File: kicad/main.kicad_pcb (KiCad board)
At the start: 2 copper layers, 119.4 x 99.1 mm, 41 parts, among them J1 Barrel_Jack, SW1 Reset, SW6 SW_DIP_x08, U1 KM1810VM88, U10 L7805, U11 15 MHz, U12 8255, U13 74HC273, U14 74HC244, U2 W27C512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

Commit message: Mark as v02
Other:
- board text added: "Андрій Дунай v0.2, Вересень 2023 <a@dun.ai>"
- board text removed: "Андрій Дунай v0.1, Вересень 2023 <a@dun.ai>"
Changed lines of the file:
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@@
   (gr_rect (start 15.24 -109.22) (end 134.62 -10.16)
     (stroke (width 0.2) (type default)) (fill none) (layer "Edge.Cuts"))
-  (gr_text "Андрій Дунай\nv0.1, Вересень 2023\n<a@dun.ai>" (at 113.3475 -41.275) (layer "F.SilkS")
+  (gr_text "Андрій Дунай\nv0.2, Вересень 2023\n<a@dun.ai>" (at 113.3475 -41.275) (layer "F.SilkS")
     (effects (font (size 1 1) (thickness 0.15)) (justify left bottom))
   )

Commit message: Update PCB image
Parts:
- moved C10 128.3 mm to (114.3, 94.0)
- moved C2 128.3 mm to (43.2, 39.4)
- moved C3 128.3 mm to (27.9, 62.2)
- moved C4 128.3 mm to (90.2, 29.2)
- moved C5 128.3 mm to (90.2, 61.0)
- moved C6 128.3 mm to (110.5, 38.1)
- moved C8 128.3 mm to (116.8, 76.1)
- moved C9 128.3 mm to (85.1, 94.0)
- moved H1 128.3 mm to (21.6, 114.3)
- moved H2 128.3 mm to (133.3, 114.3)
- moved J1 128.3 mm to (128.9, 33.0)
- moved J2 128.3 mm to (20.3, 43.2)
- moved LCD1 128.3 mm to (20.3, 20.3)
- moved RN3 128.3 mm to (80.0, 102.9)
- moved RN4 128.3 mm to (109.2, 102.9)
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
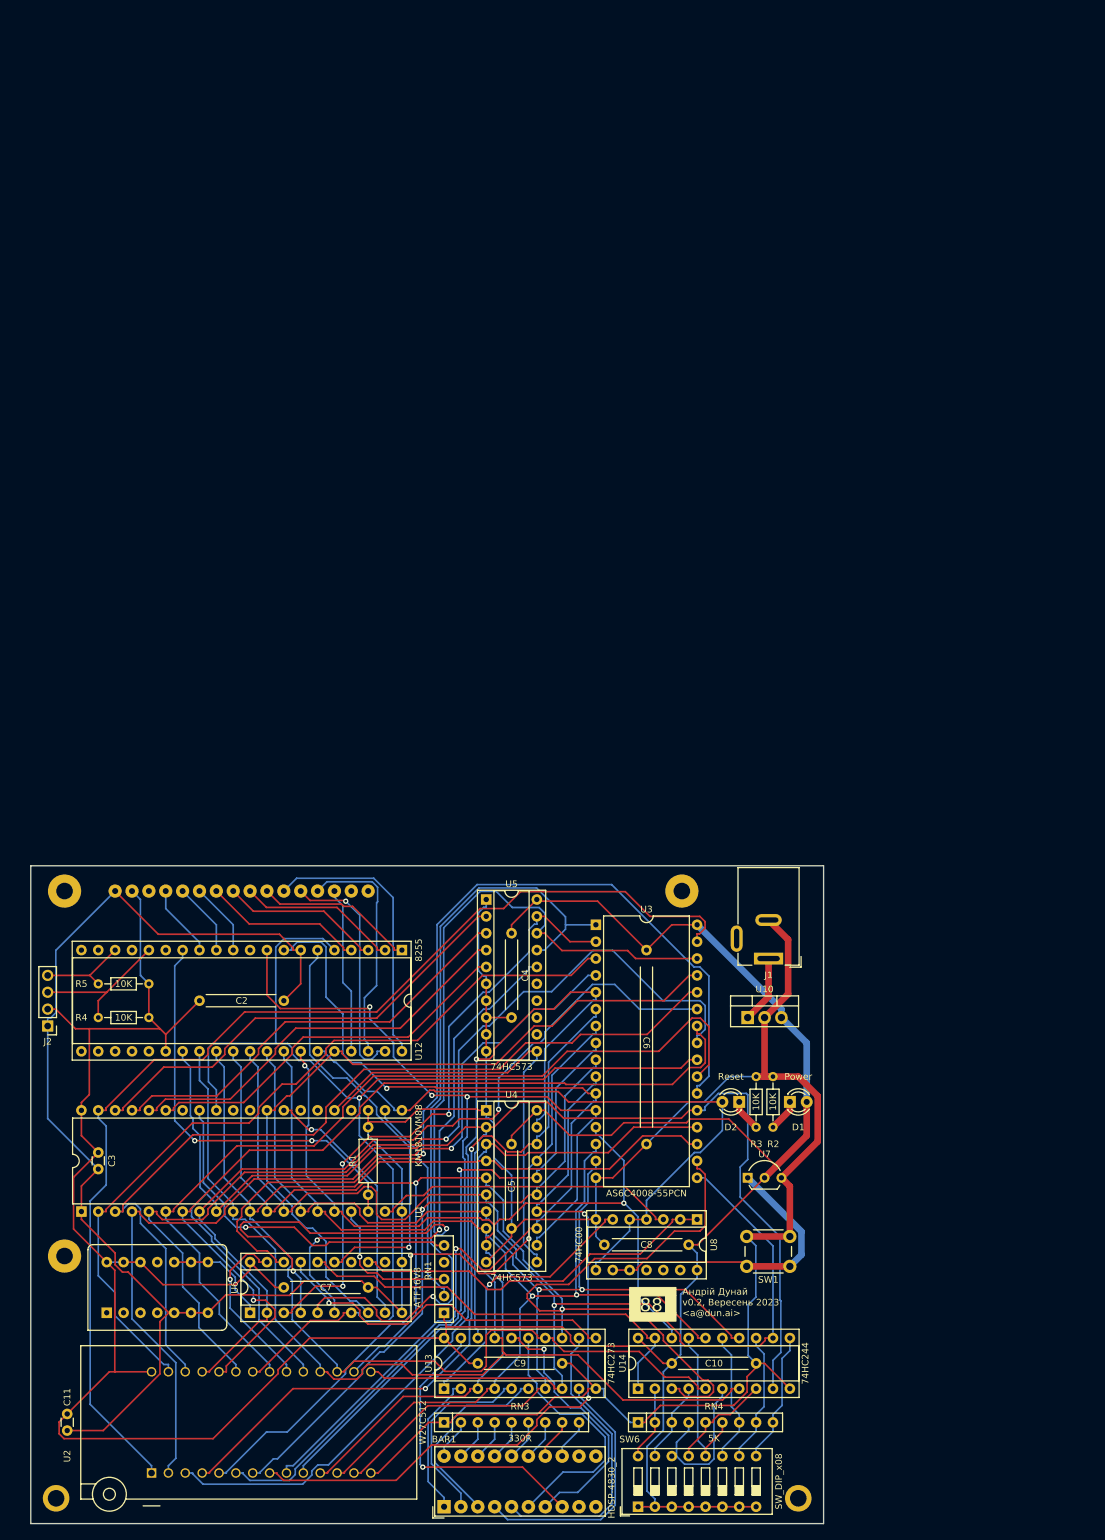
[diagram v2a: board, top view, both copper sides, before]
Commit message: Add I/O sheet
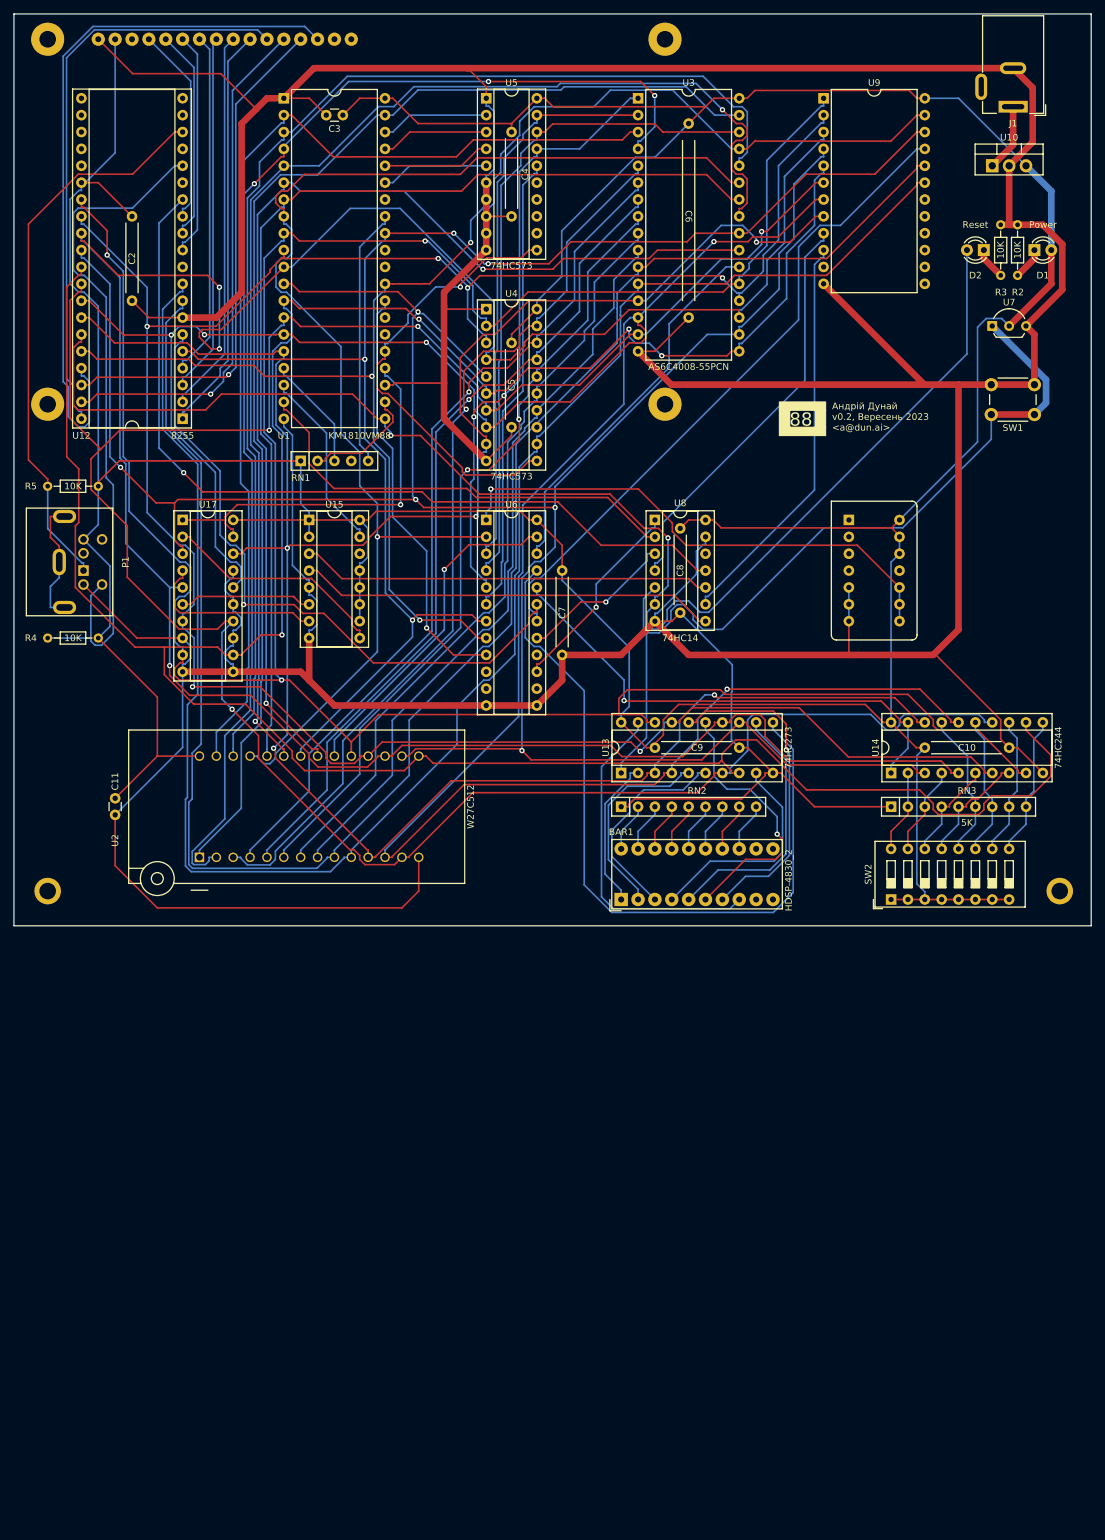
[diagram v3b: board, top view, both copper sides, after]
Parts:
- removed J2: ~, Connector_PinHeader_2.54mm:PinHeader_1x04_P2.54mm_Vertical
- removed R1: 10K, Resistor_THT:R_Axial_DIN0207_L6.3mm_D2.5mm_P10.16mm_Horizontal
- removed RN4: 5K, Resistor_THT:R_Array_SIP9
- removed SW6: SW_DIP_x08, Button_Switch_THT:SW_DIP_SPSTx08_Slide_9.78x22.5mm_W7.62mm_P2.54mm
- added P1: Mini-DIN_6pins_ver3, Custom_Footprints:Connector_Mini-DIN_Female_6Pin_2rows, F.Cu at (25.7, -25.4)
- added RN2: 330R, Resistor_THT:R_Array_SIP9, F.Cu at (106.7, 10.2)
- added SW2: SW_DIP_x08, Button_Switch_THT:SW_DIP_SPSTx08_Slide_9.78x22.5mm_W7.62mm_P2.54mm, F.Cu at (147.3, 24.1)
- added U15: 74HC148, Package_DIP:DIP-16_W7.62mm_Socket, F.Cu at (59.7, -33.0)
- added U17: 74HC244, Package_DIP:DIP-20_W7.62mm_Socket, F.Cu at (40.6, -33.0)
- added U9: 8253, Package_DIP:DIP-24_W15.24mm, F.Cu at (137.2, -96.5)
- RN3: value 330R -> 5K
- U6: value ATF16V8 -> GAL22V10; footprint Package_DIP:DIP-20_W7.62mm_Socket -> Package_DIP:DIP-24_W7.62mm_Socket
- U8: value 74HC00 -> 74HC14
- moved U1 170.4 mm to (55.9, -96.5), turned to 0 degrees
- moved C3 160.5 mm to (64.8, -94.0), turned to 180 degrees
- moved U11 152.7 mm to (144.6, -25.4), turned to -90 degrees
- moved J1 133.5 mm to (165.7, -95.2)
- moved SW1 133.5 mm to (168.9, -48.9)
- moved U7 133.5 mm to (162.6, -62.2)
- moved D1 133.5 mm to (168.9, -73.7)
- moved D2 133.5 mm to (161.3, -73.7)
- moved R2 133.5 mm to (166.4, -69.8)
- moved R3 133.5 mm to (163.8, -69.8)
- moved U10 133.5 mm to (162.6, -86.4)
- moved RN1 130.1 mm to (58.4, -41.9), turned to 0 degrees
- moved LCD1 128.3 mm to (17.8, -108.0)
- moved C6 124.6 mm to (116.8, -86.4)
- moved U3 124.6 mm to (109.2, -96.5)
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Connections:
- BAR1 pad 13: Net-(RN3-R8) -> Net-(RN2-R8)
- BAR1 pad 14: Net-(RN3-R7) -> Net-(RN2-R7)
- BAR1 pad 15: Net-(RN3-R6) -> Net-(RN2-R6)
- BAR1 pad 16: Net-(RN3-R5) -> Net-(RN2-R5)
- BAR1 pad 17: Net-(RN3-R4) -> Net-(RN2-R4)
- BAR1 pad 18: Net-(RN3-R3) -> Net-(RN2-R3)
- BAR1 pad 19: Net-(RN3-R2) -> Net-(RN2-R2)
- BAR1 pad 20: Net-(RN3-R1) -> Net-(RN2-R1)
- SW1 pad 1: Net-(U7-~{RST}) -> ~{RES}
- U1 pad 18: INT -> INTR
- U1 pad 24: unconnected-(U1-~{INTA}-Pad24) -> ~{INTA}
- U12 pad 14: INT -> Net-(U12-PC0)
- U13 pad 1: Net-(U13-~{Mr}) -> ~{RES}
- U14 pad 11: Net-(RN4-R8) -> Net-(RN3-R8)
- U14 pad 13: Net-(RN4-R7) -> Net-(RN3-R7)
- U14 pad 15: Net-(RN4-R6) -> Net-(RN3-R6)
- U14 pad 17: Net-(RN4-R5) -> Net-(RN3-R5)
- U14 pad 2: Net-(RN4-R1) -> Net-(RN3-R1)
- U14 pad 4: Net-(RN4-R2) -> Net-(RN3-R2)
- U14 pad 6: Net-(RN4-R3) -> Net-(RN3-R3)
- U14 pad 8: Net-(RN4-R4) -> Net-(RN3-R4)
- U6 pad 10: GND -> unconnected-(U6-I-Pad10)
- U6 pad 11: GND -> unconnected-(U6-I-Pad11)
- U6 pad 12: unconnected-(U6-IO8-Pad12) -> GND
- U6 pad 13: Net-(U6-IO7) -> GND
- U6 pad 15: IO~{EN} -> Net-(U6-I/O/Q-Pad15)
- U6 pad 16: IN~{EN} -> unconnected-(U6-I/O/Q-Pad16)
- U6 pad 17: OUT~{EN} -> Net-(U6-I/O/Q-Pad17)
- U6 pad 18: RAM~{EN} -> TIMER~{EN}
- U6 pad 19: ROM~{EN} -> IO~{EN}
- U6 pad 20: +5V -> IN~{EN}
- U7 pad 1: Net-(U7-~{RST}) -> ~{RES}
- U8 pad 1: Net-(U6-IO7) -> Net-(U6-I/O/Q-Pad15)
- U8 pad 10: Net-(U7-~{RST}) -> ~{INT1}
- U8 pad 11: unconnected-(U8-Pad11) -> Net-(U12-PC0)
- U8 pad 13: unconnected-(U8-Pad13) -> GND
- U8 pad 2: Net-(U6-IO7) -> CLK
- U8 pad 3: CLK -> Net-(U6-I/O/Q-Pad17)
- U8 pad 4: RES -> TIMERCLK
- U8 pad 5: RES -> ~{RES}
- U8 pad 6: Net-(U13-~{Mr}) -> RES
- U8 pad 8: RES -> ~{INT0}
- U8 pad 9: Net-(U7-~{RST}) -> Net-(U9-OUT0)
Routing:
- net GND: track 528.8 -> 921.6 mm
- net AD_{3}: track 194.8 -> 424.7 mm, vias 1 -> 4
- net AD_{1}: track 166.1 -> 384.2 mm, vias 2 -> 5
- net +5V: track 482.1 -> 683.4 mm
- net AD_{2}: track 176.7 -> 375.4 mm, vias 2 -> 4
- net AD_{5}: track 196.6 -> 391.9 mm, vias 0 -> 3
- net AD_{7}: track 231.3 -> 416.6 mm, vias 0 -> 3
- net AD_{0}: track 167.7 -> 347.5 mm, vias 2 -> 5
- net AD_{4}: track 208.0 -> 376.2 mm, vias 2 -> 5
- net AD_{6}: track 196.3 -> 357.9 mm, vias 0 -> 6
- net Net-(U12-PC0): track 0.00 -> 128.8 mm, vias 0 -> 1
- net ~{RES}: track 0.00 -> 126.5 mm
- net A_{1}: track 152.0 -> 270.9 mm, vias 2 -> 0
- net A_{0}: track 158.5 -> 273.4 mm, vias 3 -> 0
- net RES: track 102.4 -> 210.3 mm, vias 0 -> 2
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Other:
- board size 119.4 x 99.1 mm -> 162.2 x 137.3 mm

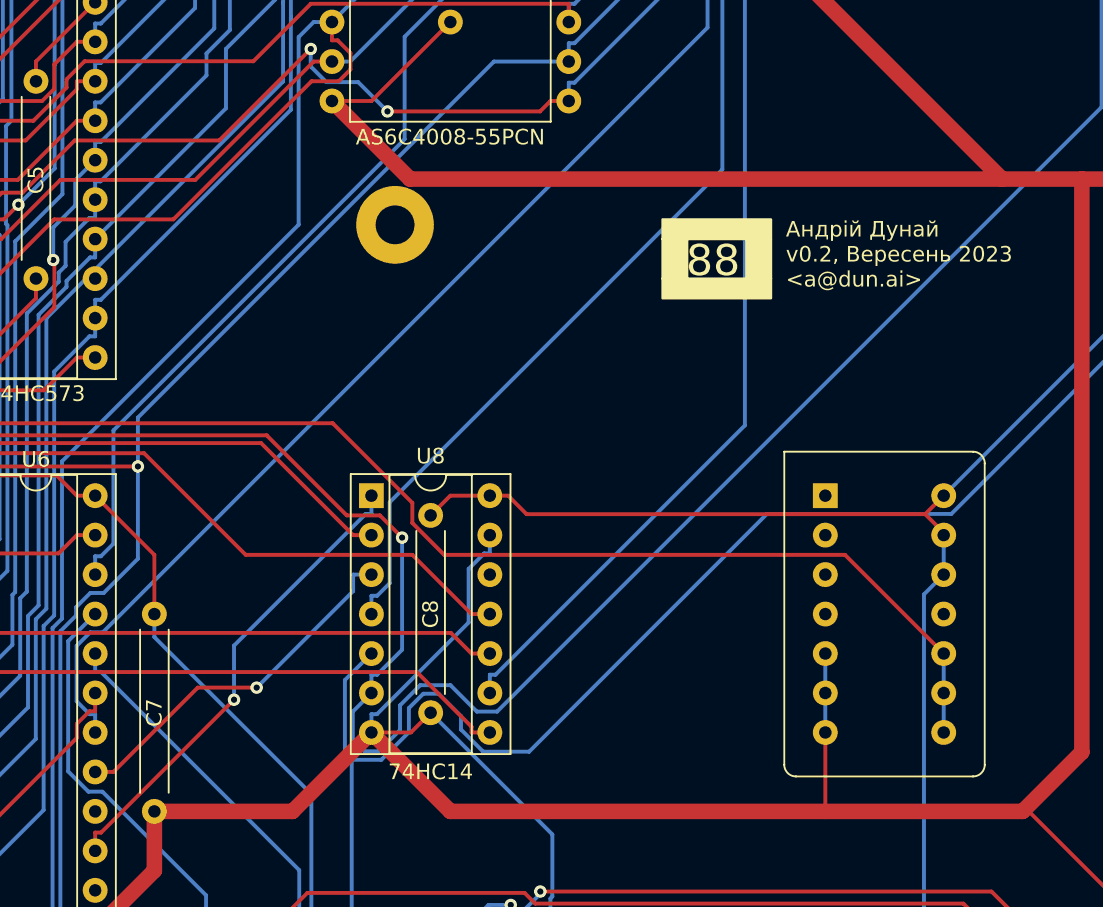
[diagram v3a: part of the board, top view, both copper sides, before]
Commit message: Tie HOLD low, add GAL simulation for clock, add 8253 clock
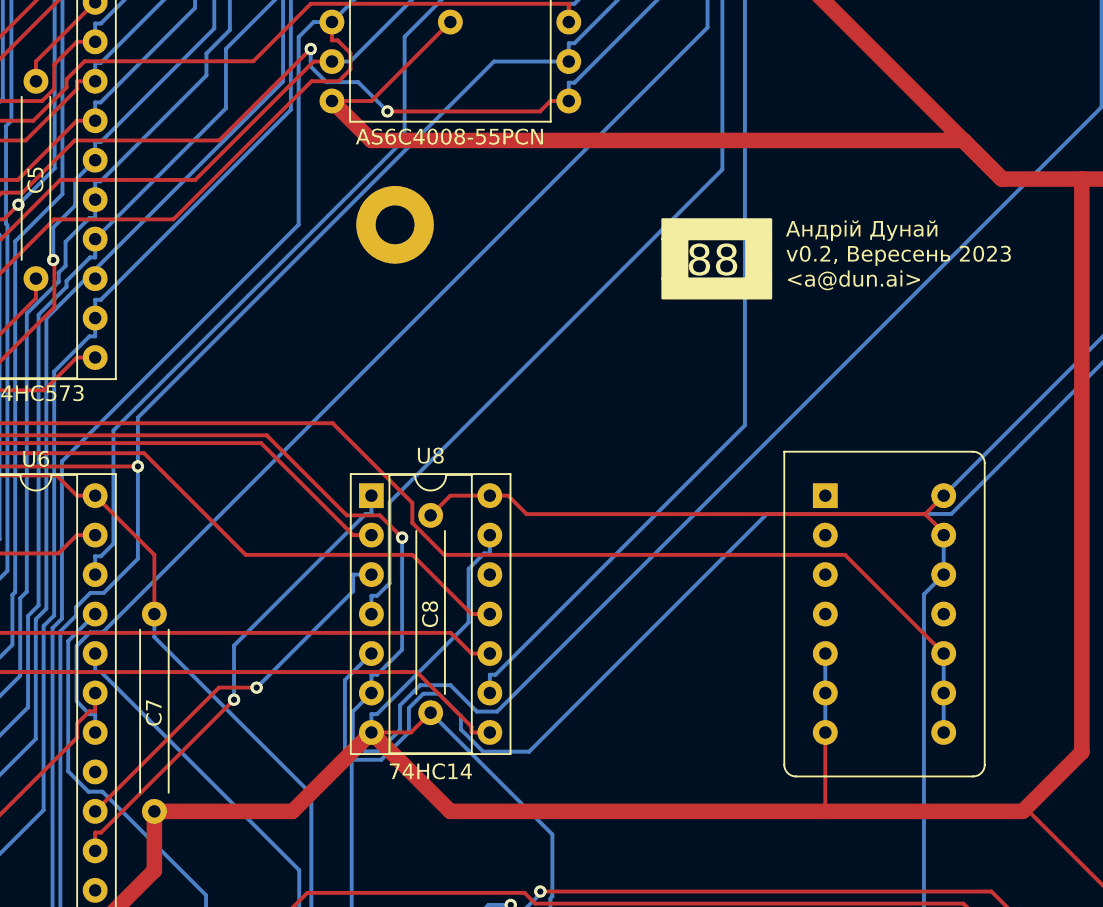
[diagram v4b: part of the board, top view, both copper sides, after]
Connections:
- U1 pad 31: unconnected-(U1-HOLD-Pad31) -> GND
- U6 pad 16: unconnected-(U6-I/O/Q-Pad16) -> Net-(U6-I/O/Q-Pad16)
- U6 pad 17: Net-(U6-I/O/Q-Pad17) -> unconnected-(U6-I/O/Q-Pad17)
- U8 pad 3: Net-(U6-I/O/Q-Pad17) -> Net-(U6-I/O/Q-Pad16)
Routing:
- net Net-(U6-I/O/Q-Pad16): track 0.00 -> 24.7 mm, vias 0 -> 1
- net Net-(U6-I/O/Q-Pad17): track 23.7 -> 0.00 mm, vias 1 -> 0
